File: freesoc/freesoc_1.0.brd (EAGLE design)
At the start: 80 x 53.3 mm, 72 parts, among them IC1 CY8C3X66AXI, IC2 CY7C68015A, IC3 REG1117, IC4 24LC00OT, P1 M20-7820842, P5 M20-7820842, Y2 ATS240C, Y3 ST2012SB32768H5HPWAA, Y4 ATS240C

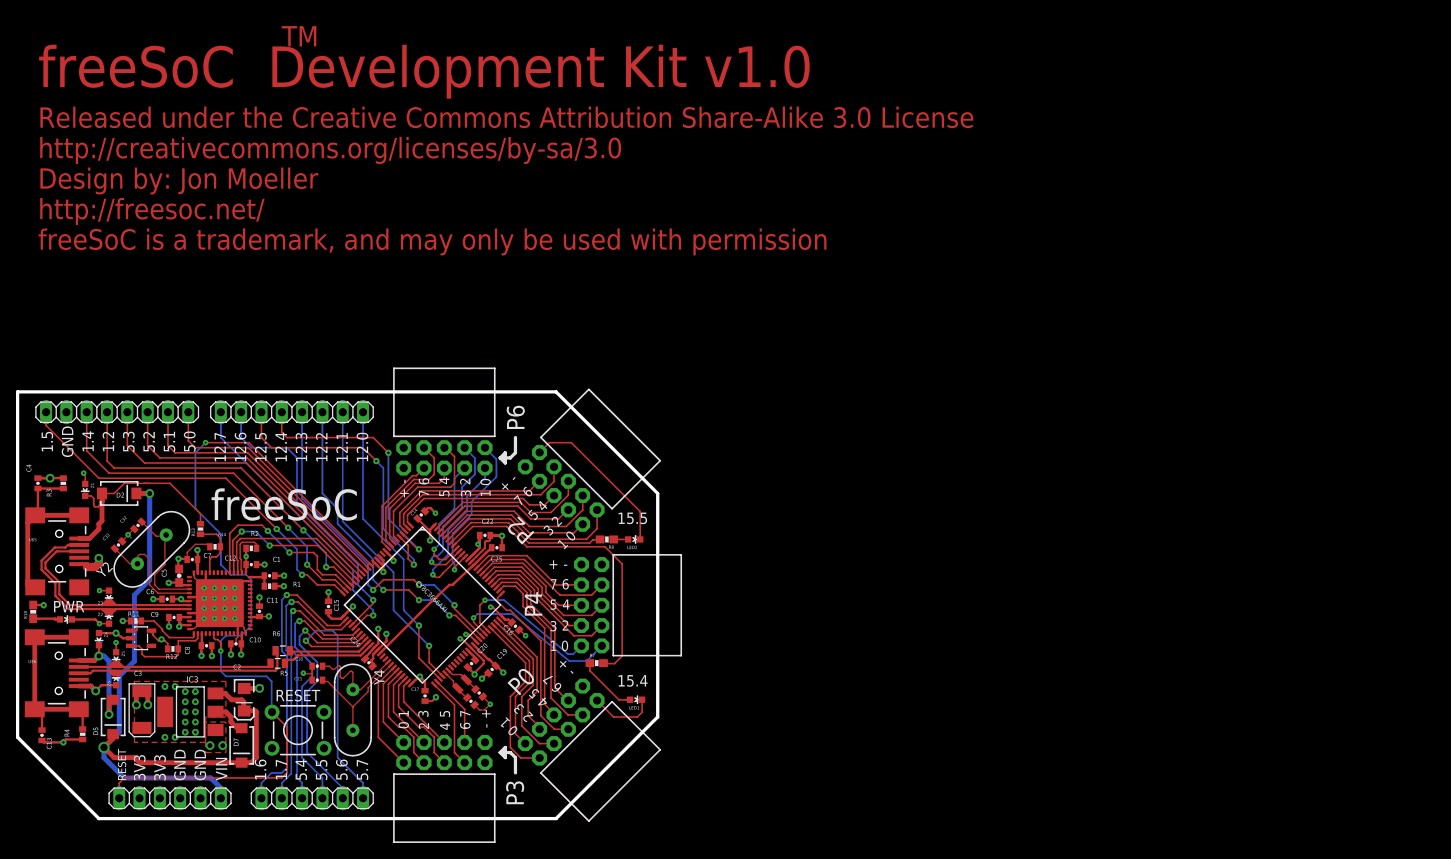
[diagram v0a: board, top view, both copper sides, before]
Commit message: DFM changes to freeSoC
Updated board for 7/7mil trace/space.

All vias are now tented.

Updated FX2 QFN pad land for improved reliability
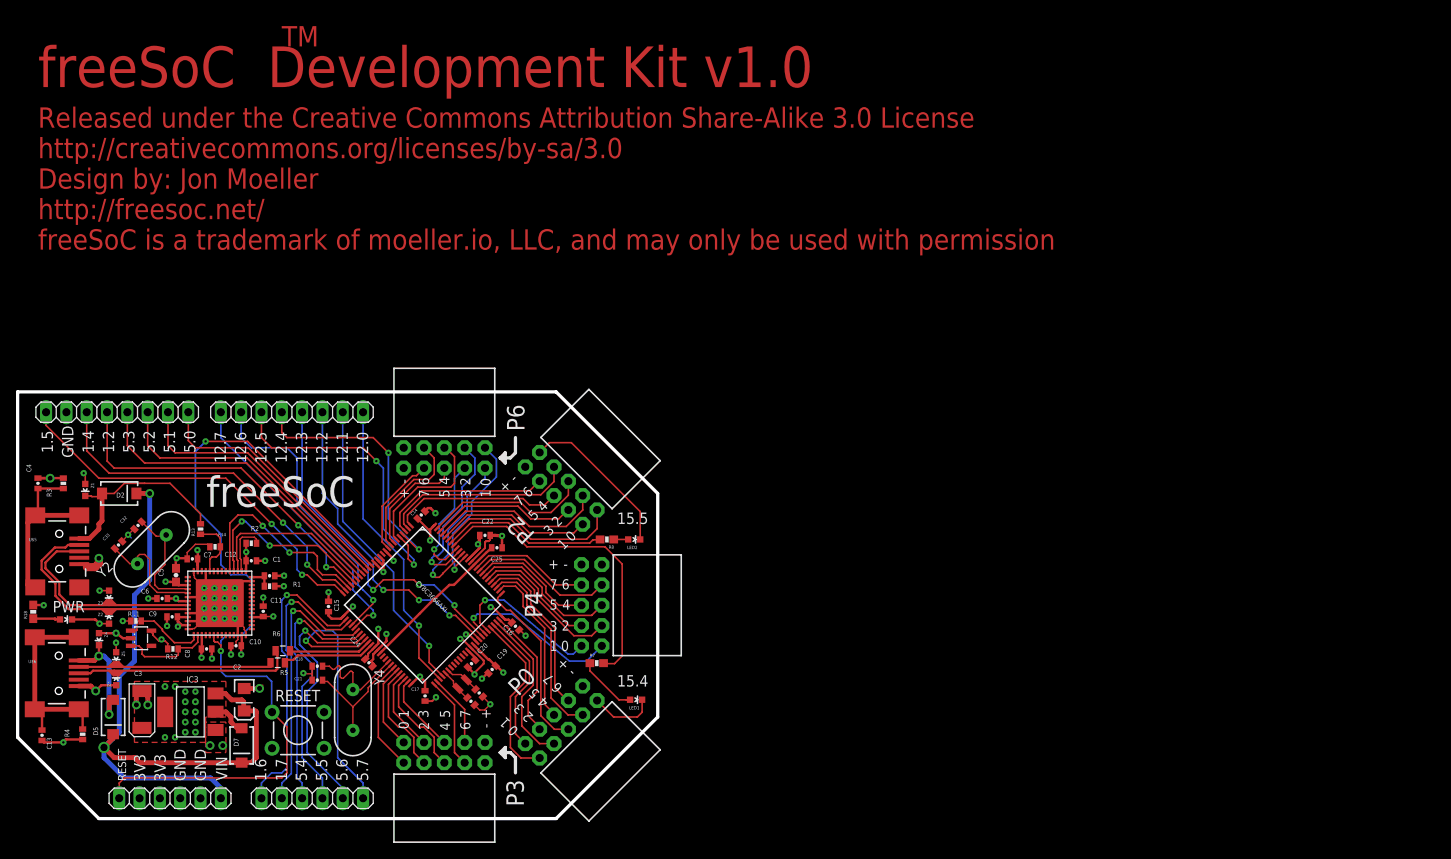
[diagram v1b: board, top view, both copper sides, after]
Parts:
- moved C6 0.64 mm to (38.4, 30.1)
- moved R2 0.63 mm to (49.5, 37.0)
- moved C11 0.48 mm to (51.0, 28.4)
- moved C12 0.48 mm to (49.5, 34.8)
- moved C5 0.40 mm to (40.1, 33.0)
- moved C8 0.40 mm to (43.9, 23.7)
- moved C9 0.25 mm to (39.6, 27.8)
- moved C10 0.24 mm to (47.6, 24.1)
- moved C7 0.08 mm to (42.2, 35.0)
- moved R5 0.08 mm to (52.8, 22.0)
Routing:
- net VDD: track 73.9 -> 77.0 mm
- net VBUS1: track 31.1 -> 28.8 mm
- net GND: track 170.7 -> 172.6 mm
- net SWO: track 24.4 -> 26.0 mm
- net SWDCK: track 22.3 -> 23.9 mm
- net SWDIO: track 21.2 -> 21.9 mm
- net EESCL: track 10.8 -> 11.3 mm
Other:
- board text added: "freeSoC is a trademark of moeller.io, LLC, and may only be used with permission"
- board text removed: "freeSoC is a trademark, and may only be used with permission"

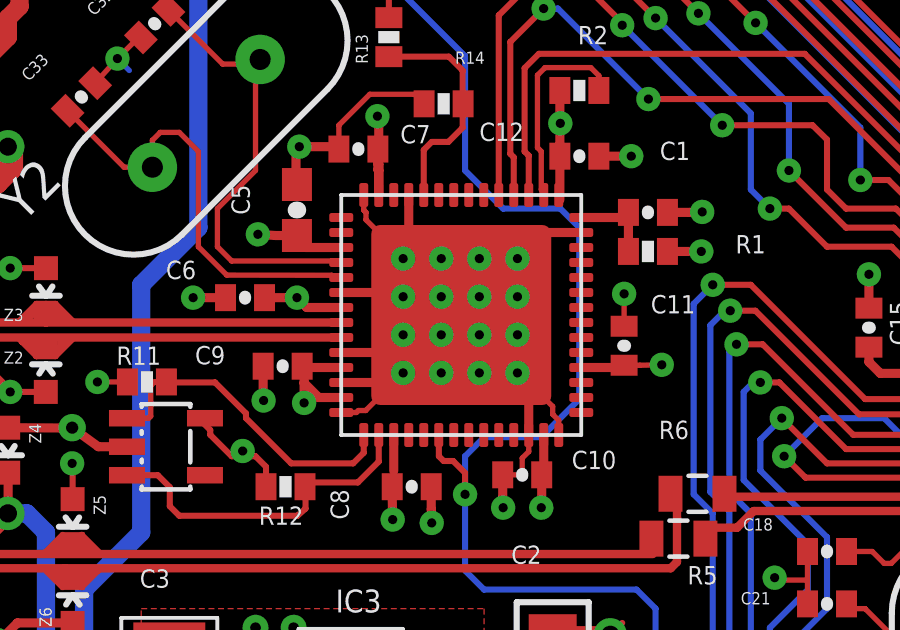
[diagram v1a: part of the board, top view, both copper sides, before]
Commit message: More DFM changes
Updated FX2 QFN package thermal pad dimensions to meet Cypress spec.

Added tented vias on thermal pad, appropriate solder paste mask, and
opened vias on bottom to eliminate outgassing
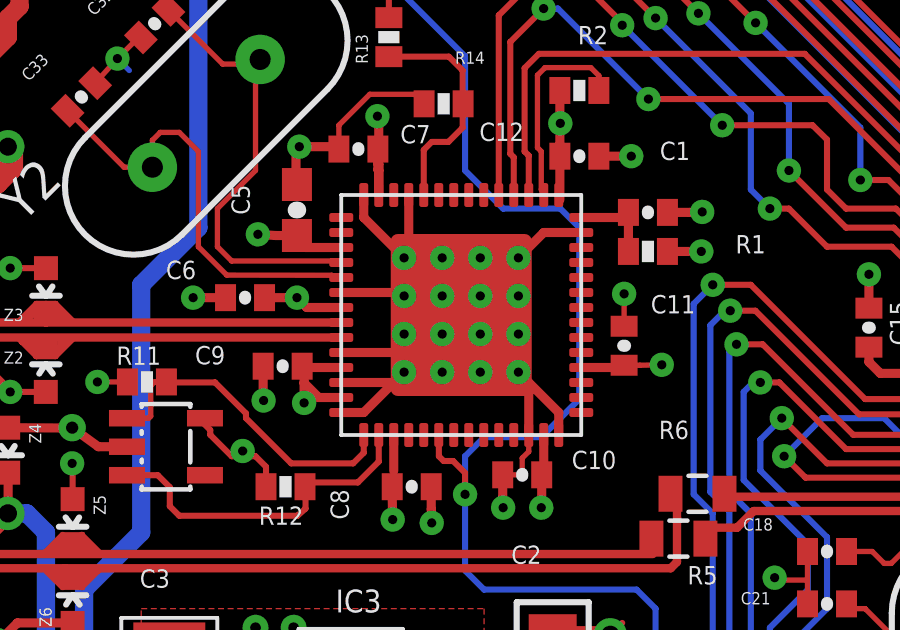
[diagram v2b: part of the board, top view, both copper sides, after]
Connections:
- net GND: now also IC2.P$1, IC2.P$10, IC2.P$11, IC2.P$12, IC2.P$13, IC2.P$14, IC2.P$15, IC2.P$16, IC2.P$2, IC2.P$3, IC2.P$4, IC2.P$5, IC2.P$6, IC2.P$7, IC2.P$8, IC2.P$9
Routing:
- net GND: track 172.6 -> 161.9 mm, vias 53 -> 37
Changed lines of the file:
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@@
 <layer number="28" name="bValues" color="7" fill="1" visible="yes" active="yes"/>
 <layer number="29" name="tStop" color="2" fill="3" visible="yes" active="yes"/>
-<layer number="30" name="bStop" color="5" fill="6" visible="no" active="yes"/>
+<layer number="30" name="bStop" color="5" fill="6" visible="yes" active="yes"/>
 <layer number="31" name="tCream" color="7" fill="4" visible="yes" active="yes"/>
 <layer number="32" name="bCream" color="7" fill="5" visible="yes" active="yes"/>
@@
 <via x="51.260375" y="34.76625" extent="1-16" drill="0.3048"/>
 <wire x1="49.593" y1="32.223021875" x2="48.343" y2="32.223021875" width="0.3048" layer="1"/>
-<wire x1="48.343" y1="32.223021875" x2="45.593" y2="29.473021875" width="0.1778" layer="1"/>
 <wire x1="51.02225" y1="29.098" x2="51.02225" y2="30.178375" width="0.1778" layer="1"/>
 <via x="51.02225" y="30.178375" extent="1-16" drill="0.3048"/>
 <wire x1="47.843" y1="25.473021875" x2="47.843" y2="27.223021875" width="0.3048" layer="1"/>
-<wire x1="47.843" y1="27.223021875" x2="45.593" y2="29.473021875" width="0.1778" layer="1"/>
-<wire x1="48.843" y1="25.473021875" x2="48.843" y2="25.96" width="0.1778" layer="1"/>
-<wire x1="48.843" y1="25.96" x2="48.641" y2="26.162" width="0.1778" layer="1"/>
-<wire x1="48.641" y1="26.162" x2="48.641" y2="26.425021875" width="0.1778" layer="1"/>
-<wire x1="48.641" y1="26.425021875" x2="45.593" y2="29.473021875" width="0.1778" layer="1"/>
-<wire x1="41.593" y1="26.223021875" x2="42.098021875" y2="26.223021875" width="0.1778" layer="1"/>
-<wire x1="42.098021875" y1="26.223021875" x2="42.164" y2="26.289" width="0.1778" layer="1"/>
-<wire x1="42.164" y1="26.289" x2="42.408978125" y2="26.289" width="0.1778" layer="1"/>
-<wire x1="42.408978125" y1="26.289" x2="45.593" y2="29.473021875" width="0.1778" layer="1"/>
+<wire x1="47.843" y1="27.223021875" x2="47.498" y2="27.568021875" width="0.1778" layer="1"/>
+<wire x1="47.498" y1="27.568021875" x2="45.593" y2="29.473021875" width="0.1778" layer="1"/>
 <wire x1="41.593" y1="27.223021875" x2="43.343" y2="27.223021875" width="0.3048" layer="1"/>
-<wire x1="43.343" y1="27.223021875" x2="45.593" y2="29.473021875" width="0.1778" layer="1"/>
+<wire x1="43.343" y1="27.223021875" x2="43.688" y2="27.568021875" width="0.1778" layer="1"/>
+<wire x1="43.688" y1="27.568021875" x2="45.593" y2="29.473021875" width="0.1778" layer="1"/>
 <wire x1="41.593" y1="28.223021875" x2="44.343" y2="28.223021875" width="0.3048" layer="1"/>
 <wire x1="44.343" y1="28.223021875" x2="45.593" y2="29.473021875" width="0.1778" layer="1"/>
@@
 <wire x1="43.843" y1="33.473021875" x2="43.843" y2="31.223021875" width="0.3048" layer="1"/>
 <wire x1="43.843" y1="31.223021875" x2="45.593" y2="29.473021875" width="0.1778" layer="1"/>
-<wire x1="42.343" y1="33.473021875" x2="42.343" y2="32.968" width="0.1778" layer="1"/>
-<wire x1="42.343" y1="32.968" x2="42.418" y2="32.893" width="0.1778" layer="1"/>
-<wire x1="42.418" y1="32.893" x2="42.418" y2="32.648021875" width="0.1778" layer="1"/>
-<wire x1="42.418" y1="32.648021875" x2="45.593" y2="29.473021875" width="0.1778" layer="1"/>
 <wire x1="46.975" y1="24.145875" x2="47.498" y2="24.145875" width="0.1778" layer="1"/>
 <wire x1="47.498" y1="24.145875" x2="47.625" y2="24.272875" width="0.1778" layer="1"/>
@@
 <wire x1="35.861625" y1="18.476625" x2="36.591875" y2="17.746375" width="0.6096" layer="1" curve="-90"/>
 <wire x1="36.591875" y1="17.746375" x2="36.591875" y2="16.748125" width="0.6096" layer="1"/>
-<via x="43.65625" y="31.353125" extent="1-16" drill="0.3048"/>
-<via x="44.92625" y="31.353125" extent="1-16" drill="0.3048"/>
-<via x="46.19625" y="31.353125" extent="1-16" drill="0.3048"/>
-<via x="47.46625" y="31.353125" extent="1-16" drill="0.3048"/>
-<via x="43.65625" y="30.083125" extent="1-16" drill="0.3048"/>
-<via x="44.92625" y="30.083125" extent="1-16" drill="0.3048"/>
-<via x="46.19625" y="30.083125" extent="1-16" drill="0.3048"/>
-<via x="47.46625" y="30.083125" extent="1-16" drill="0.3048"/>
-<via x="47.46625" y="28.813125" extent="1-16" drill="0.3048"/>
-<via x="46.19625" y="28.813125" extent="1-16" drill="0.3048"/>
-<via x="44.92625" y="28.813125" extent="1-16" drill="0.3048"/>
-<via x="43.65625" y="28.813125" extent="1-16" drill="0.3048"/>
-<via x="43.65625" y="27.543125" extent="1-16" drill="0.3048"/>
-<via x="44.92625" y="27.543125" extent="1-16" drill="0.3048"/>
-<via x="46.19625" y="27.543125" extent="1-16" drill="0.3048"/>
-<via x="47.46625" y="27.543125" extent="1-16" drill="0.3048"/>
 <wire x1="98.38125" y1="17.399" x2="98.38125" y2="15.83125" width="0.2032" layer="1"/>
 <wire x1="98.38125" y1="15.83125" x2="97.79" y2="15.24" width="0.2032" layer="1"/>
@@
 <wire x1="30.56" y1="26.90875" x2="30.559375" y2="26.908125" width="0.3048" layer="1"/>
 <wire x1="34.835015625" y1="38.724390625" x2="34.914390625" y2="38.724390625" width="0.1778" layer="1"/>
+<contactref element="IC2" pad="P$1"/>
+<contactref element="IC2" pad="P$2"/>
+<contactref element="IC2" pad="P$3"/>
+<contactref element="IC2" pad="P$4"/>
+<contactref element="IC2" pad="P$5"/>
+<contactref element="IC2" pad="P$6"/>
+<contactref element="IC2" pad="P$7"/>
+<contactref element="IC2" pad="P$8"/>
+<contactref element="IC2" pad="P$9"/>
+<contactref element="IC2" pad="P$10"/>
+<contactref element="IC2" pad="P$11"/>
+<contactref element="IC2" pad="P$12"/>
+<contactref element="IC2" pad="P$13"/>
+<contactref element="IC2" pad="P$14"/>
+<contactref element="IC2" pad="P$15"/>
+<contactref element="IC2" pad="P$16"/>
+<wire x1="41.593" y1="26.223021875" x2="42.343" y2="26.223021875" width="0.3048" layer="1"/>
+<wire x1="42.343" y1="26.223021875" x2="43.688" y2="27.568021875" width="0.3048" layer="1"/>
+<wire x1="48.843" y1="25.473021875" x2="48.843" y2="26.223021875" width="0.3048" layer="1"/>
+<wire x1="48.843" y1="26.223021875" x2="47.498" y2="27.568021875" width="0.3048" layer="1"/>
+<wire x1="48.343" y1="32.223021875" x2="47.498" y2="31.378021875" width="0.3048" layer="1"/>
+<wire x1="42.343" y1="33.473021875" x2="42.343" y2="32.723021875" width="0.3048" layer="1"/>
+<wire x1="42.343" y1="32.723021875" x2="43.688" y2="31.378021875" width="0.3048" layer="1"/>
 </signal>
 <signal name="VIN">

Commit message: Updates to boards for production
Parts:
- removed C13: 10nF, SparkFun:0402-CAP
- removed IC3: REG1117, burr-brown:SOT223
- removed P1, P5: M20-7820842, pinhead:1X08
- removed R4: 100k, SparkFun:0402-RES
- added C23: 10uF, SparkFun:1206
- added D1, D3: STPS1L30A, SparkFun:SMA-DIODE
- added JP10, JP7, JP8, JP9: M20-7820842, SparkFun:1X08
- added JP6: 455-1749-1-ND, SparkFun:JST-2-SMD
- added U$1: LP2989, SparkFun:SO08
- C2: value 10uF -> 10nF C0G; device SparkFun:EIA3216 -> SparkFun:0402-CAP
- C3: value 100uF -> 10uF; device SparkFun:EIA6032 -> SparkFun:1206
- moved R18 29.2 mm to (49.7, 18.5), turned to 180 degrees
- moved LED5 26.7 mm to (50.1, 15.1), turned to 180 degrees
- moved D7 9.68 mm to (42.6, 19.5), turned to 180 degrees
- moved Z1 5.15 mm to (32.8, 40.4), turned to 90 degrees
- moved C4 4.45 mm to (27.3, 44.5)
- moved C3 4.42 mm to (39.7, 14.0)
- moved C2 3.64 mm to (45.0, 17.2), turned to 0 degrees
- moved D5 3.21 mm to (34.9, 17.0), turned to 0 degrees
- moved R3 2.78 mm to (28.8, 44.5)
- moved U$6 1.91 mm to (25.4, 22.6)
- moved Z4 1.84 mm to (30.7, 26.8)
- moved Z2 1.11 mm to (32.9, 27.7)
- moved Z3 1.11 mm to (32.9, 30.3)
- moved R11 0.90 mm to (35.8, 26.6)
- moved U$5 0.65 mm to (25.4, 36.6)
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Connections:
- removed net N$10: C4.2, R3.2, U$5.MTN1, U$5.MTN2, U$5.MTN3
- removed net N$16: C13.2, R4.2, U$6.MTN1, U$6.MTN2, U$6.MTN3, U$6.MTN4
- new net N$13: C2.1, U$1.1
- new net N$2: D1.A, JP6.2
- new net SHIELD: C4.2, R3.2, U$5.MTN1, U$5.MTN2, U$5.MTN3, U$6.MTN1, U$6.MTN2, U$6.MTN3, U$6.MTN4
- net GND: now also C2.2, C23.2, C3.2, D3.A, JP6.1, JP7.2, JP9.2, U$1.3; no longer C13.1, C2.C, C3.P$2, IC3.1, P5.7, R4.1
- net P12: now also JP7.4, JP9.4; no longer P5.5
- net P120: now also JP10.8, JP8.8; no longer P1.1
- net P121: now also JP10.7, JP8.7; no longer P1.2
- net P122: now also JP10.6, JP8.6; no longer P1.3
- net P123: now also JP10.5, JP8.5; no longer P1.4
- net P124: now also JP10.4, JP8.4; no longer P1.5
- net P125: now also JP10.3, JP8.3; no longer P1.6
- net P126: now also JP10.2, JP8.2; no longer P1.7
- net P127: now also JP10.1, JP8.1; no longer P1.8
- net P14: now also JP7.3, JP9.3; no longer P5.6
- net P15: now also JP7.1, JP9.1; no longer P5.8
- net P50: now also JP7.8, JP9.8; no longer P5.1
- net P51: now also JP7.7, JP9.7; no longer P5.2
- net P52: now also JP7.6, JP9.6; no longer P5.3
- net P53: now also JP7.5, JP9.5; no longer P5.4
- net VDD: now also C23.1, U$1.5, U$1.6; no longer C3.P$1, IC3.2, IC3.4
- net VIN: now also C3.1, D1.C, D3.C, U$1.4, U$1.8; no longer C2.A, IC3.3
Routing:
- net SHIELD: track 0.00 -> 46.1 mm
- net N$16: track 26.0 -> 0.00 mm, vias 0 -> 1
- net N$10: track 22.3 -> 0.00 mm, vias 0 -> 1
- net GND: track 161.9 -> 179.7 mm, vias 37 -> 32
- net !XRES: track 108.5 -> 90.8 mm
- net VDD: track 77.0 -> 83.9 mm, vias 33 -> 19
- net VIN: track 89.2 -> 82.4 mm
- net P127: track 36.3 -> 43.0 mm
- net N$2: track 0.00 -> 4.93 mm
- net P67: track 12.8 -> 16.2 mm
- net P126: track 37.2 -> 40.5 mm
- net P15: track 49.0 -> 52.0 mm, vias 2 -> 3
- net N$13: track 0.00 -> 2.92 mm
- net EESCL: track 11.3 -> 14.0 mm
- net D-: track 37.7 -> 35.5 mm
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- removed copper zone on layer 1, net GND
- removed copper zone on layer 1, net VDD
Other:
- outline, holes or cut-outs redrawn
- board text added: "RST"
- board text removed: "PWR"
